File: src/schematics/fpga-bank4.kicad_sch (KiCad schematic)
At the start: 1 part

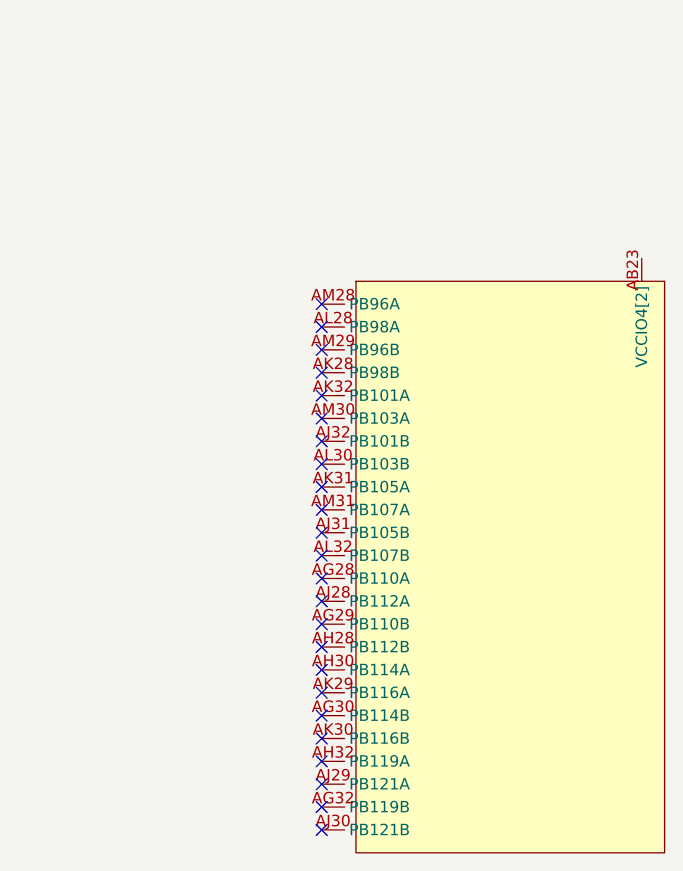
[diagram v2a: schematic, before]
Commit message: ✨ Replace some LVDS diff pairs with 3v3 single-ended signals (#56)
* ✨ Replace some LVDS diff pairs with 3v3 single-ended signals

* Finishes replacing LVDS diff pairs with 3v3 single ended
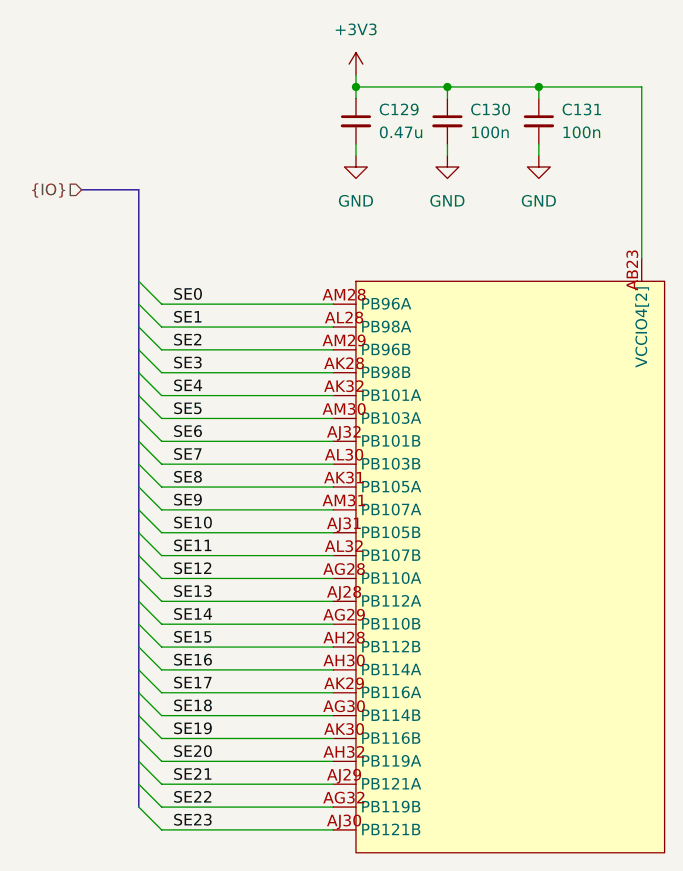
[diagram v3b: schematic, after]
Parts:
- added C129: 0.47u, symbol Device:C_Small
- added C130, C131: 100n, symbol Device:C_Small
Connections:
- net +3V3: now reaches U6.AB23 (VCCIO4[2]), U6.AC23 (VCCIO4)
- net +3V3: now also C129.1, C130.1, C131.1
- net SE12: now reaches U6.AG28 (PB110A)
- net SE14: now reaches U6.AG29 (PB110B)
- net SE18: now reaches U6.AG30 (PB114B)
- net SE22: now reaches U6.AG32 (PB119B)
- net SE15: now reaches U6.AH28 (PB112B)
- net SE16: now reaches U6.AH30 (PB114A)
- net SE20: now reaches U6.AH32 (PB119A)
- net SE13: now reaches U6.AJ28 (PB112A)
- net SE21: now reaches U6.AJ29 (PB121A)
- net SE23: now reaches U6.AJ30 (PB121B)
- net SE10: now reaches U6.AJ31 (PB105B)
- net SE6: now reaches U6.AJ32 (PB101B)
- net SE3: now reaches U6.AK28 (PB98B)
- net SE17: now reaches U6.AK29 (PB116A)
- net SE19: now reaches U6.AK30 (PB116B)
- net SE8: now reaches U6.AK31 (PB105A)
- net SE4: now reaches U6.AK32 (PB101A)
- net SE1: now reaches U6.AL28 (PB98A)
- net SE7: now reaches U6.AL30 (PB103B)
- net SE11: now reaches U6.AL32 (PB107B)
- net SE0: now reaches U6.AM28 (PB96A)
- net SE2: now reaches U6.AM29 (PB96B)
- net SE5: now reaches U6.AM30 (PB103A)
- net SE9: now reaches U6.AM31 (PB107A)
- new net GND: C129.2, C130.2, C131.2
- no-connect marks 24 -> 0

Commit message: Add footprint for ecp5 (#75)
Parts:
- U6: footprint (none) -> ECAP5-DPROC:LFE5U-85F-_BG756C
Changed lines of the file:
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@@
 			)
 		)
-		(property "Footprint" ""
+		(property "Footprint" "ECAP5-DPROC:LFE5U-85F-_BG756C"
 			(at 138.43 71.12 0)
 			(effects

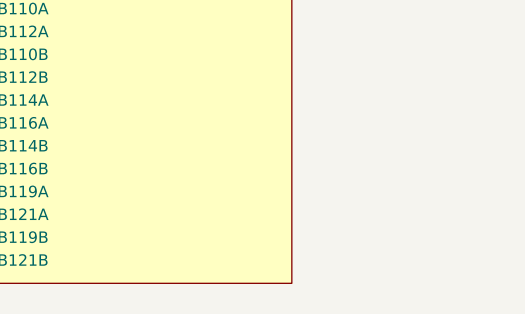
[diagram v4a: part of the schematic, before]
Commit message: Add footprint for the io connector
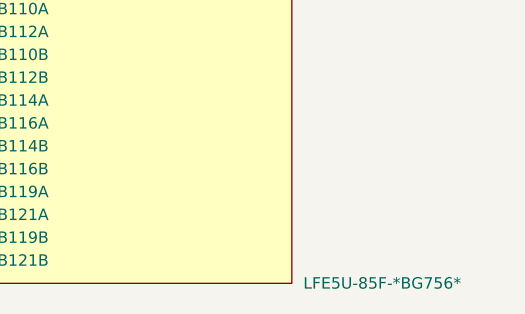
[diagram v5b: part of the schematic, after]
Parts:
- U6: value ~ -> LFE5U-85F-*BG756*
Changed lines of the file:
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@@
 			)
 		)
-		(property "Value" "~"
+		(property "Value" "LFE5U-85F-*BG756*"
 			(at 171.45 132.08 0)
 			(effects

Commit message: Add remaining component footprints (#79)
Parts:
- C129, C130, C131: footprint (none) -> Capacitor_SMD:C_0402_1005Metric
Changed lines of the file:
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@@
 			)
 		)
-		(property "Footprint" ""
+		(property "Footprint" "Capacitor_SMD:C_0402_1005Metric"
 			(at 135.89 50.8 0)
 			(effects
@@
 			)
 		)
-		(property "Footprint" ""
+		(property "Footprint" "Capacitor_SMD:C_0402_1005Metric"
 			(at 156.21 50.8 0)
 			(effects
@@
 			)
 		)
-		(property "Footprint" ""
+		(property "Footprint" "Capacitor_SMD:C_0402_1005Metric"
 			(at 146.05 50.8 0)
 			(effects

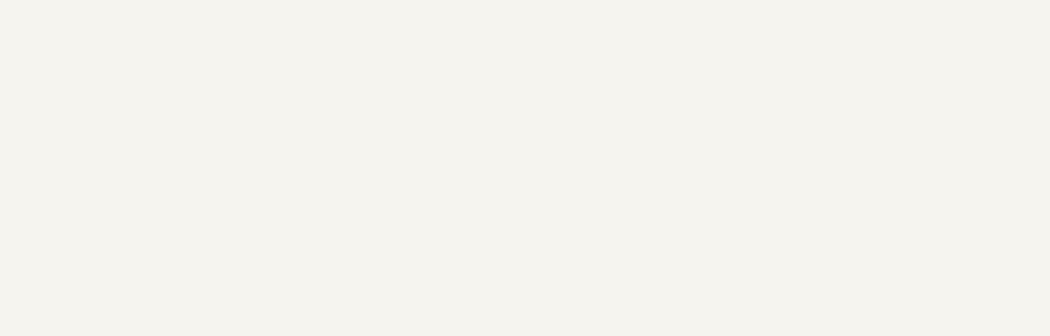
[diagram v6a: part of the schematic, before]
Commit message: Add notes on the schematic
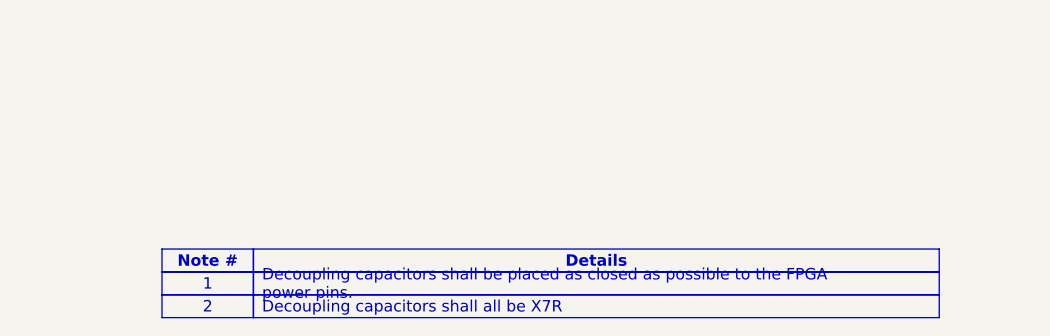
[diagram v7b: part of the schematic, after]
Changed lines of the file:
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@@
 		(comment 3 "${Part Number}")
+	)
+	(text_box "Note #"
+		(exclude_from_sim no)
+		(at 193.04 162.56 0)
+		(size 10.16 2.54)
+		(margins 0.9525 0.9525 0.9525 0.9525)
+		(stroke
+			(width 0)
+			(type solid)
+			(color 0 0 0 1)
+		)
+		(fill
+			(type none)
+		)
+		(effects
+			(font
+				(face "Arial")
+				(size 1.27 1.27)
+				(bold yes)
+				(color 0 0 0 1)
+			)
+		)
+	)
+	(text_box "Decoupling capacitors shall be placed as closed as possible to the FPGA power pins."
+		(exclude_from_sim no)
+		(at 203.2 165.1 0)
+		(size 76.2 2.54)
+		(margins 0.9525 0.9525 0.9525 0.9525)
+		(stroke
+			(width 0)
+			(type solid)
+			(color 0 0 0 1)
+		)
+		(fill
+			(type none)
+		)
+		(effects
+			(font
+				(face "Arial")
+				(size 1.27 1.27)
+				(color 0 0 0 1)
+			)
+			(justify left)
+		)
+	)
+	(text_box "Details"
+		(exclude_from_sim no)
+		(at 203.2 162.56 0)
+		(size 76.2 2.54)
+		(margins 0.9525 0.9525 0.9525 0.9525)
+		(stroke
+			(width 0)
+			(type solid)
+			(color 0 0 0 1)
+		)
+		(fill
+			(type none)
+		)
+		(effects
+			(font
+				(face "Arial")
+				(size 1.27 1.27)
+				(bold yes)
+				(color 0 0 0 1)
+			)
+		)
+	)
+	(text_box "2"
+		(exclude_from_sim no)
+		(at 193.04 167.64 0)
+		(size 10.16 2.54)
+		(margins 0.9525 0.9525 0.9525 0.9525)
+		(stroke
+			(width 0)
+			(type solid)
+			(color 0 0 0 1)
+		)
+		(fill
+			(type none)
+		)
+		(effects
+			(font
+				(face "Arial")
+				(size 1.27 1.27)
+				(color 0 0 0 1)
+			)
+		)
+	)
+	(text_box "1"
+		(exclude_from_sim no)
+		(at 193.04 165.1 0)
+		(size 10.16 2.54)
+		(margins 0.9525 0.9525 0.9525 0.9525)
+		(stroke
+			(width 0)
+			(type solid)
+			(color 0 0 0 1)
+		)
+		(fill
+			(type none)
+		)
+		(effects
+			(font
+				(face "Arial")
+				(size 1.27 1.27)
+				(color 0 0 0 1)
+			)
+		)
+	)
+	(text_box "Decoupling capacitors shall all be X7R"
+		(exclude_from_sim no)
+		(at 203.2 167.64 0)
+		(size 76.2 2.54)
+		(margins 0.9525 0.9525 0.9525 0.9525)
+		(stroke
+			(width 0)
+			(type solid)
+			(color 0 0 0 1)
+		)
+		(fill
+			(type none)
+		)
+		(effects
+			(font
+				(face "Arial")
+				(size 1.27 1.27)
+				(color 0 0 0 1)
+			)
+			(justify left)
+		)
 	)
 	(junction

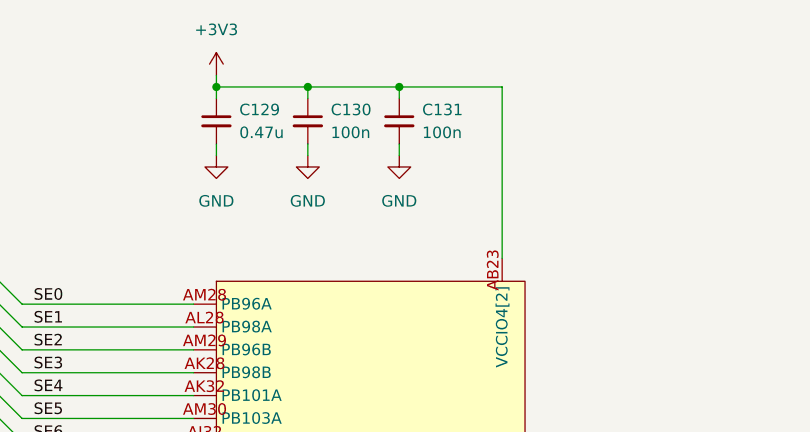
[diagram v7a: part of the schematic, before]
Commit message: Route the board power supply (#89)
* Replaces the inductors for smaller ones

* Starts routing the power supply

* Starts routing power

* Start adding power planes

* Adds decoupling capacitors

* Adds routing of the power sequencing

* Add routing for SRAM

* Route the SRAM data pins

* Finish routing the SRAM

* Route the SDRAM

* Move 1.8v converter to other side of the board

* Start routing DDR2 data lanes

* Use 0402 resistors instead of 0201 for emmc termination

* Route signals from DDR2 to FPGA bank

* Update routing of emmc

* Route the DDR2 without length matching

* Add length matching for DDR on L4 and L6. Todo L1 and redo L6

* Update routing of DDR2 L6 traces. Todo L1

* Finish routing of ddr2 traces

* Update power layer to support stripline for ddr2

* Fixed mechanical holes
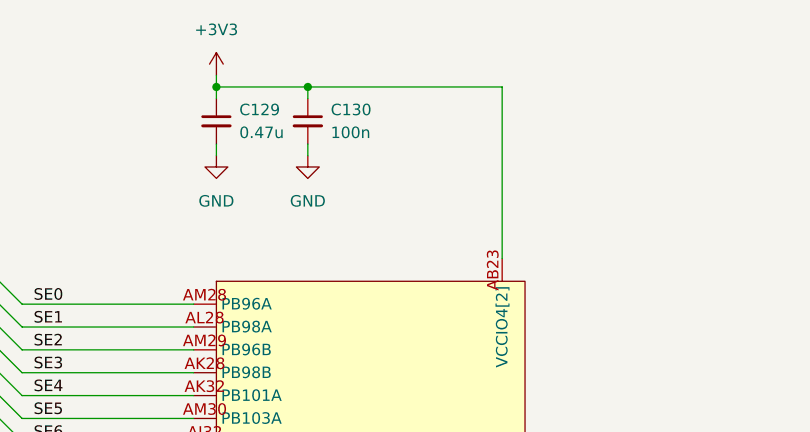
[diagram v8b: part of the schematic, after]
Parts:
- removed C131: 100n, Capacitor_SMD:C_0402_1005Metric, symbol Device:C_Small
- C129, C130: footprint Capacitor_SMD:C_0402_1005Metric -> Capacitor_SMD:C_0201_0603Metric
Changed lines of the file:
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@@
-		(color 0 0 0 0)
-	)
-	(junction
-		(at 156.21 46.99)
-		(diameter 0)
 		(color 0 0 0 0)
 	)
@@
 	(wire
 		(pts
-			(xy 146.05 46.99) (xy 156.21 46.99)
-		)
-		(stroke
-			(width 0)
-			(type default)
-		)
-	)
-	(wire
-		(pts
-			(xy 156.21 53.34) (xy 156.21 54.61)
-		)
-		(stroke
-			(width 0)
-			(type default)
-		)
-	)
-	(wire
-		(pts
-			(xy 167.64 46.99) (xy 156.21 46.99)
+			(xy 146.05 46.99) (xy 167.64 46.99)
 		)
 		(stroke
@@
 		(pts
 			(xy 111.76 114.3) (xy 111.76 116.84)
-		)
-		(stroke
-			(width 0)
-			(type default)
-		)
-	)
-	(wire
-		(pts
-			(xy 156.21 46.99) (xy 156.21 48.26)
 		)
 		(stroke
@@
 	(symbol
 		(lib_id "power:GND")
-		(at 156.21 54.61 0)
-		(unit 1)
-		(exclude_from_sim no)
-		(in_bom yes)
-		(on_board yes)
-		(dnp no)
-		(fields_autoplaced yes)
-		(property "Reference" "#PWR0163"
-			(at 156.21 60.96 0)
-			(effects
-				(font
-					(size 1.27 1.27)
-				)
-				(hide yes)
-			)
-		)
-		(property "Value" "GND"
-			(at 156.21 59.69 0)
-			(effects
-				(font
-					(size 1.27 1.27)
-				)
-			)
-		)
-		(property "Footprint" ""
-			(at 156.21 54.61 0)
-			(effects
-				(font
-					(size 1.27 1.27)
-				)
-				(hide yes)
-			)
-		)
-		(property "Datasheet" ""
-			(at 156.21 54.61 0)
-			(effects
-				(font
-					(size 1.27 1.27)
-				)
-				(hide yes)
-			)
-		)
-		(property "Description" "Power symbol creates a global label with name \"GND\" , ground"
-			(at 156.21 54.61 0)
-			(effects
-				(font
-					(size 1.27 1.27)
-				)
-				(hide yes)
-			)
-		)
-		(pin "1"
-		)
-		(instances
-			(project "ecap5-bsom"
-				(path "/c5fd18a3-9aa0-4151-b6e0-94da3d606686/cf7b4afe-be2f-4770-95a4-78e3e4d23437"
-					(reference "#PWR0163")
-					(unit 1)
-				)
-			)
-		)
-	)
-	(symbol
-		(lib_id "power:GND")
 		(at 135.89 54.61 0)
 		(unit 1)
@@
 			)
 		)
-		(property "Footprint" "Capacitor_SMD:C_0402_1005Metric"
+		(property "Footprint" "Capacitor_SMD:C_0201_0603Metric"
 			(at 135.89 50.8 0)
 			(effects
@@
 				(path "/c5fd18a3-9aa0-4151-b6e0-94da3d606686/cf7b4afe-be2f-4770-95a4-78e3e4d23437"
 					(reference "C129")
-					(unit 1)
-				)
-			)
-		)
-	)
-	(symbol
-		(lib_id "Device:C_Small")
-		(at 156.21 50.8 0)
-		(unit 1)
-		(exclude_from_sim no)
-		(in_bom yes)
-		(on_board yes)
-		(dnp no)
-		(fields_autoplaced yes)
-		(property "Reference" "C131"
-			(at 158.75 49.5362 0)
-			(effects
-				(font
-					(size 1.27 1.27)
-				)
-				(justify left)
-			)
-		)
-		(property "Value" "100n"
-			(at 158.75 52.0762 0)
-			(effects
-				(font
-					(size 1.27 1.27)
-				)
-				(justify left)
-			)
-		)
-		(property "Footprint" "Capacitor_SMD:C_0402_1005Metric"
-			(at 156.21 50.8 0)
-			(effects
-				(font
-					(size 1.27 1.27)
-				)
-				(hide yes)
-			)
-		)
-		(property "Datasheet" "~"
-			(at 156.21 50.8 0)
-			(effects
-				(font
-					(size 1.27 1.27)
-				)
-				(hide yes)
-			)
-		)
-		(property "Description" "Unpolarized capacitor, small symbol"
-			(at 156.21 50.8 0)
-			(effects
-				(font
-					(size 1.27 1.27)
-				)
-				(hide yes)
-			)
-		)
-		(pin "1"
-		)
-		(pin "2"
-		)
-		(instances
-			(project "ecap5-bsom"
-				(path "/c5fd18a3-9aa0-4151-b6e0-94da3d606686/cf7b4afe-be2f-4770-95a4-78e3e4d23437"
-					(reference "C131")
 					(unit 1)
 				)
@@
 			)
 		)
-		(property "Footprint" "Capacitor_SMD:C_0402_1005Metric"
+		(property "Footprint" "Capacitor_SMD:C_0201_0603Metric"
 			(at 146.05 50.8 0)
 			(effects
